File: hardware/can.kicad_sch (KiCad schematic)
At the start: 4 parts, among them J1 Conn_01x04_Male, J3 Conn_01x04_Male, U6 TCAN3403

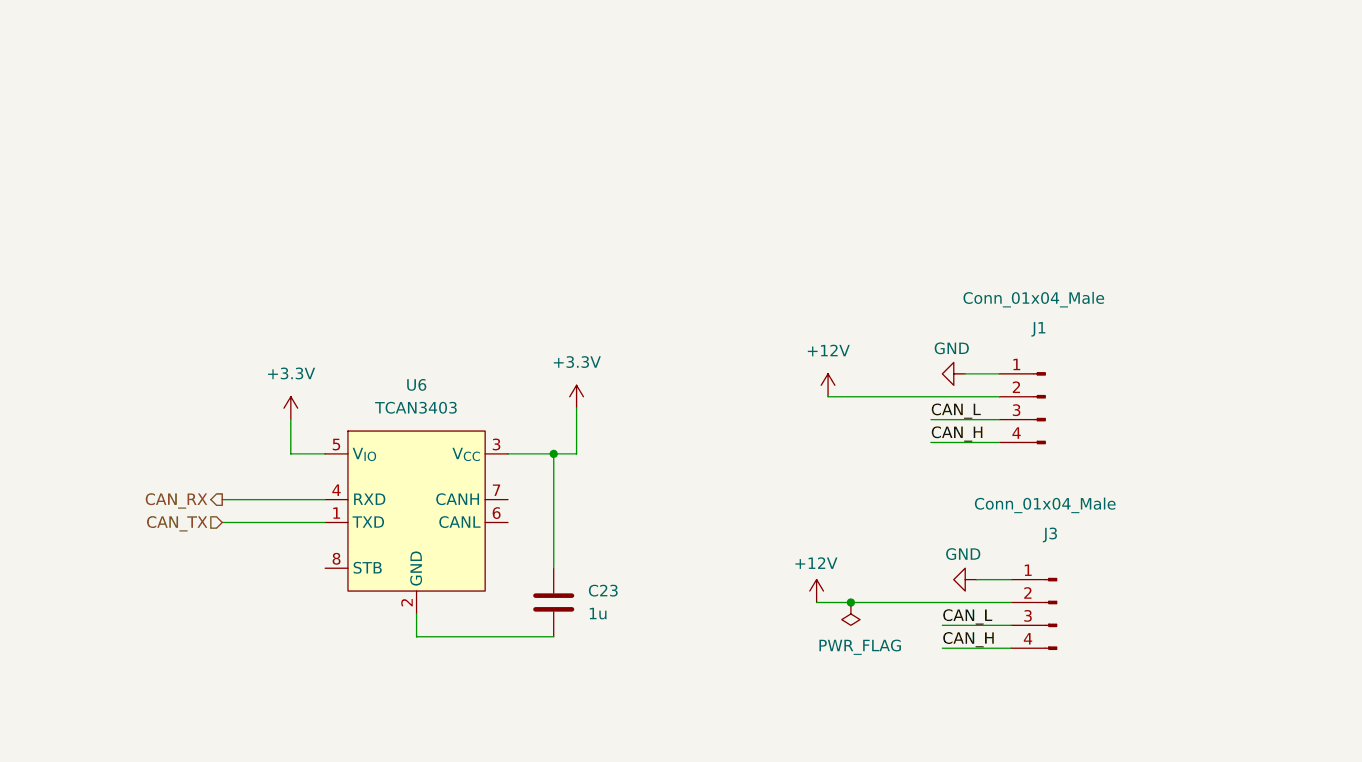
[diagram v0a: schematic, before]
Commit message: Fixed ERC errors & CAN module
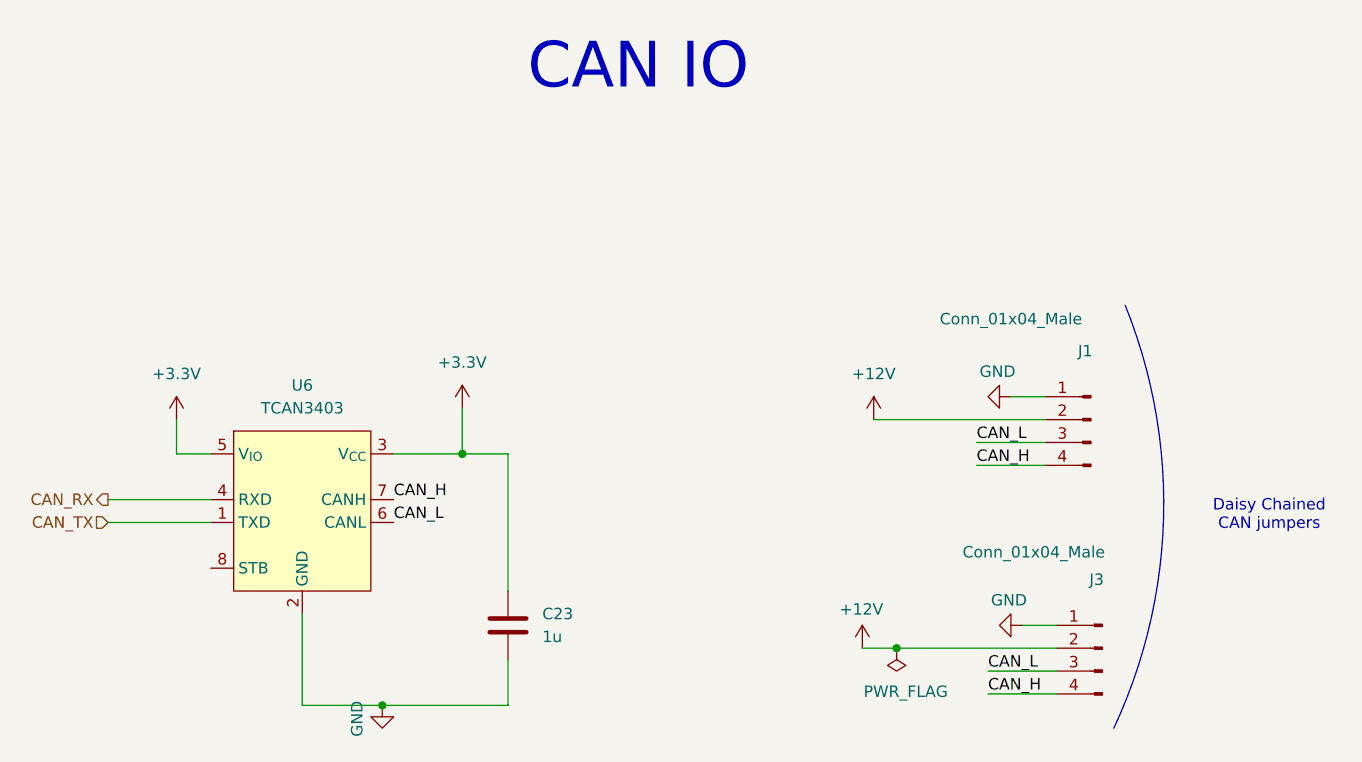
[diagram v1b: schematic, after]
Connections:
- net CAN_H: now also U6.7 (CANH)
- net CAN_L: now also U6.6 (CANL)
- net GND: now also C23.2, U6.2 (GND)
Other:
- note added: "CAN IO"
- note added: "Daisy Chained CAN jumpers"
- moved on the sheet: C23, J1, J3, U6

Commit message: Added EEPROM, resolved comments
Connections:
- net GND: now also U6.8 (STB)
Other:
- company: (none) -> University of Toronto Human Powered Vehicles
- title: (none) -> CAN I/O Interface
- moved on the sheet: C23
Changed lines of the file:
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@@
 	(generator_version "9.0")
 	(paper "A5")
+	(title_block
+		(title "CAN I/O Interface")
+		(date "2025-08-20")
+		(rev "Rev5")
+		(company "University of Toronto Human Powered Vehicles")
+	)
 	(arc
 		(start 158.75 46.99)
@@
 	)
 	(junction
-		(at 76.2 91.44)
+		(at 149.86 82.55)
 		(diameter 0)
 		(color 0 0 0 0)
 	)
+	(junction
+		(at 67.31 85.09)
+		(diameter 0)
+		(color 0 0 0 0)
+	)
 	(wire
 		(pts
@@
 	(wire
 		(pts
-			(xy 76.2 91.44) (xy 90.17 91.44)
-		)
-		(stroke
-			(width 0)
-			(type default)
-		)
-	)
-	(wire
-		(pts
 			(xy 142.24 64.77) (xy 149.86 64.77)
 		)
@@
 	(wire
 		(pts
-			(xy 90.17 63.5) (xy 90.17 78.74)
+			(xy 149.86 82.55) (xy 142.24 82.55)
+		)
+		(stroke
+			(width 0)
+			(type default)
+		)
+	)
+	(wire
+		(pts
+			(xy 85.09 63.5) (xy 85.09 73.66)
 		)
 		(stroke
@@
 	(wire
 		(pts
-			(xy 90.17 63.5) (xy 85.09 63.5)
-		)
-		(stroke
-			(width 0)
-			(type default)
-		)
-	)
-	(wire
-		(pts
-			(xy 67.31 81.28) (xy 67.31 91.44)
-		)
-		(stroke
-			(width 0)
-			(type default)
-		)
-	)
-	(wire
-		(pts
-			(xy 151.13 82.55) (xy 147.32 82.55)
+			(xy 67.31 85.09) (xy 67.31 91.44)
+		)
+		(stroke
+			(width 0)
+			(type default)
+		)
+	)
+	(wire
+		(pts
+			(xy 67.31 81.28) (xy 67.31 85.09)
+		)
+		(stroke
+			(width 0)
+			(type default)
+		)
+	)
+	(wire
+		(pts
+			(xy 151.13 82.55) (xy 149.86 82.55)
 		)
 		(stroke
@@
 	(wire
 		(pts
-			(xy 90.17 86.36) (xy 90.17 91.44)
+			(xy 85.09 81.28) (xy 85.09 85.09)
+		)
+		(stroke
+			(width 0)
+			(type default)
+		)
+	)
+	(wire
+		(pts
+			(xy 57.15 85.09) (xy 67.31 85.09)
 		)
 		(stroke
@@
 	(wire
 		(pts
+			(xy 57.15 76.2) (xy 57.15 85.09)
+		)
+		(stroke
+			(width 0)
+			(type default)
+		)
+	)
+	(wire
+		(pts
 			(xy 143.51 87.63) (xy 151.13 87.63)
 		)
@@
 	(wire
 		(pts
-			(xy 67.31 91.44) (xy 76.2 91.44)
+			(xy 67.31 85.09) (xy 85.09 85.09)
 		)
 		(stroke
@@
 	(symbol
 		(lib_id "Device:C")
-		(at 90.17 82.55 0)
+		(at 85.09 77.47 0)
 		(unit 1)
 		(exclude_from_sim no)
@@
 		(fields_autoplaced yes)
 		(property "Reference" "C23"
-			(at 93.98 81.2799 0)
+			(at 88.9 76.1999 0)
 			(effects
 				(font
@@
 		)
 		(property "Value" "1u"
-			(at 93.98 83.8199 0)
+			(at 88.9 78.7399 0)
 			(effects
 				(font
@@
 		)
 		(property "Footprint" "Capacitor_SMD:C_0402_1005Metric"
-			(at 91.1352 86.36 0)
+			(at 86.0552 81.28 0)
 			(effects
 				(font
@@
 		)
 		(property "Datasheet" "~"
-			(at 90.17 82.55 0)
+			(at 85.09 77.47 0)
 			(effects
 				(font
@@
 		)
 		(property "Description" "Unpolarized capacitor"
-			(at 90.17 82.55 0)
+			(at 85.09 77.47 0)
 			(effects
 				(font
@@
 		)
 		(property "LCSC" "C52923"
-			(at 90.17 82.55 0)
+			(at 85.09 77.47 0)
 			(effects
 				(font
@@
 	(symbol
 		(lib_id "power:GND")
-		(at 76.2 91.44 0)
+		(at 67.31 91.44 0)
 		(mirror y)
 		(unit 1)
@@
 		(dnp no)
 		(property "Reference" "#PWR08"
-			(at 76.2 97.79 0)
+			(at 67.31 97.79 0)
 			(effects
 				(font
@@
 		)
 		(property "Value" "GND"
-			(at 73.406 90.932 90)
+			(at 64.516 90.932 90)
 			(effects
 				(font
@@
 		)
 		(property "Footprint" ""
-			(at 76.2 91.44 0)
+			(at 67.31 91.44 0)
 			(effects
 				(font
@@
 		)
 		(property "Datasheet" ""
-			(at 76.2 91.44 0)
+			(at 67.31 91.44 0)
 			(effects
 				(font
@@
 		)
 		(property "Description" "Power symbol creates a global label with name \"GND\" , ground"
-			(at 76.2 91.44 0)
+			(at 67.31 91.44 0)
 			(effects
 				(font
@@
 	(symbol
 		(lib_id "power:GND")
-		(at 147.32 82.55 270)
+		(at 142.24 82.55 270)
 		(mirror x)
 		(unit 1)
@@
 		(dnp no)
 		(property "Reference" "#PWR011"
-			(at 140.97 82.55 0)
+			(at 135.89 82.55 0)
 			(effects
 				(font
@@
 		)
 		(property "Value" "GND"
-			(at 147.828 79.756 90)
+			(at 142.748 79.756 90)
 			(effects
 				(font
@@
 		)
 		(property "Footprint" ""
-			(at 147.32 82.55 0)
+			(at 142.24 82.55 0)
 			(effects
 				(font
@@
 		)
 		(property "Datasheet" ""
-			(at 147.32 82.55 0)
+			(at 142.24 82.55 0)
 			(effects
 				(font
@@
 		)
 		(property "Description" "Power symbol creates a global label with name \"GND\" , ground"
-			(at 147.32 82.55 0)
+			(at 142.24 82.55 0)
 			(effects
 				(font
@@
 					(unit 1)
 				)
+			)
+		)
+	)
+	(symbol
+		(lib_id "power:PWR_FLAG")
+		(at 149.86 82.55 0)
+		(unit 1)
+		(exclude_from_sim no)
+		(in_bom yes)
+		(on_board yes)
+		(dnp no)
+		(property "Reference" "#FLG04"
+			(at 149.86 80.645 0)
+			(effects
+				(font
+					(size 1.27 1.27)
+				)
+				(hide yes)
+			)
+		)
+		(property "Value" "PWR_FLAG"
+			(at 148.844 77.724 0)
+			(effects
+				(font
+					(size 1.27 1.27)
+				)
+			)
+		)
+		(property "Footprint" ""
+			(at 149.86 82.55 0)
+			(effects
+				(font
+					(size 1.27 1.27)
+				)
+				(hide yes)
+			)
+		)
+		(property "Datasheet" "~"
+			(at 149.86 82.55 0)
+			(effects
+				(font
+					(size 1.27 1.27)
+				)
+				(hide yes)
+			)
+		)
+		(property "Description" "Special symbol for telling ERC where power comes from"
+			(at 149.86 82.55 0)
+			(effects
+				(font
+					(size 1.27 1.27)
+				)
+				(hide yes)
+			)
+		)
+		(pin "1"
+		)
+		(instances
+			(project "flight_stick"
+				(path "/594f9b09-cd7b-4dfb-a8eb-b099e26ad96c/ff15c41c-b8ff-467f-9236-a212997d9f2b"
+					(reference "#FLG04")
+					(unit 1)
+				)

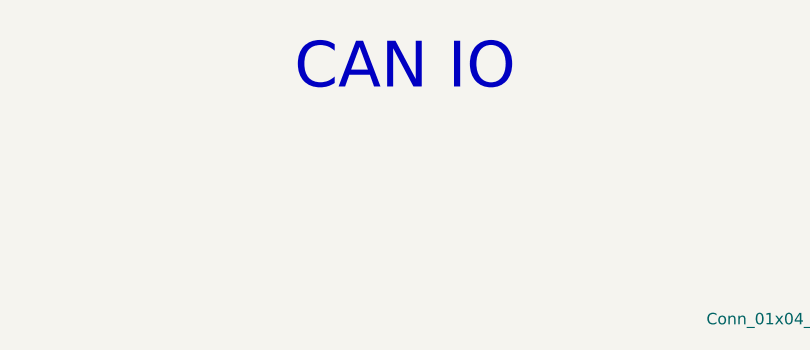
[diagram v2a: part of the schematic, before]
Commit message: revamped button matrix
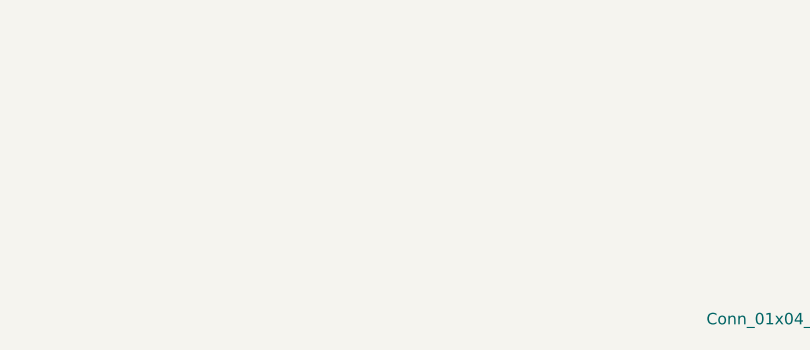
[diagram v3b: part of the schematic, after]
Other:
- note removed: "CAN IO"
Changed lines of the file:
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@@
-		)
-	)
-	(text "CAN IO"
-		(exclude_from_sim no)
-		(at 104.648 20.574 0)
-		(effects
-			(font
-				(size 5.08 5.08)
-			)
 		)
 	)

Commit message: Resolved comments
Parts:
- C23: LCSC C52923 -> C15849
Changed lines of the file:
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@@
 			)
 		)
-		(property "LCSC" "C52923"
+		(property "LCSC" "C15849"
 			(at 85.09 77.47 0)
 			(effects

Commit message: changed 0402 cap part # and regenerated prod files
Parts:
- C23: LCSC C15849 -> C29266
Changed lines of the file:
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@@
 			)
 		)
-		(property "LCSC" "C15849"
+		(property "LCSC" "C29266"
 			(at 85.09 77.47 0)
 			(effects
